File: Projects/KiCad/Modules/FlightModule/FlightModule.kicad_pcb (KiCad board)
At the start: 2 copper layers, 110 x 95 mm, 72 parts, among them J1 Conn_01x08, J2 Conn_01x02_Pin, J3 Conn_01x02_Pin, J4 Conn_01x02_Pin, J5 Conn_01x02_Pin, J6 Conn_01x02_Pin, Q1 Q_NPN_BEC, Q2 Q_NPN_BEC, SW1 SW_DIP_x02, U1 MCP2562-E-P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

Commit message: ブザーの回路を修正
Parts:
- moved BZ1 7.60 mm to (186.0, 85.7), turned to -90 degrees
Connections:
- BZ1 pad 2: GND -> Net-(BZ1-+)
- Q2 pad 3: +5V -> Net-(BZ1-+)
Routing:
- net +5V: track 110.7 -> 97.3 mm
- net Net-(BZ1-+): track 0.00 -> 9.17 mm

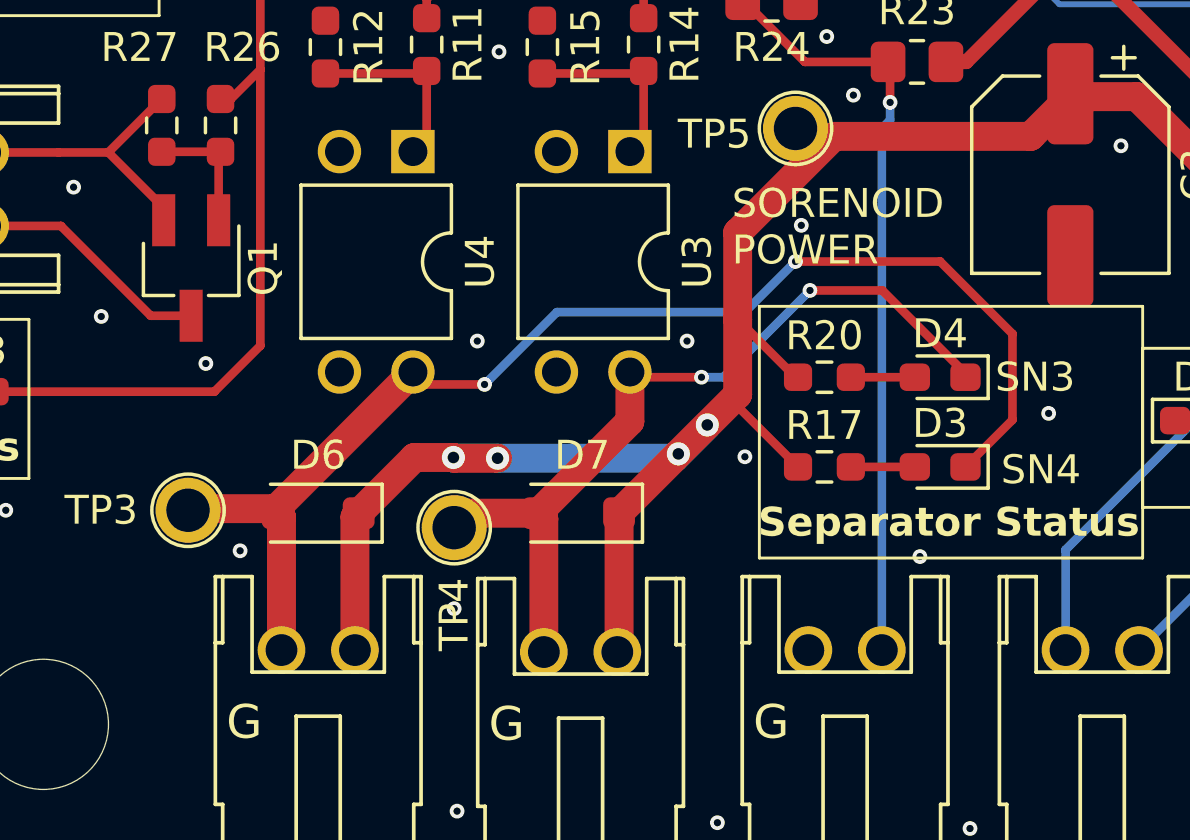
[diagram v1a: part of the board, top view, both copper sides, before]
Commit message: 電磁弁制御のフォトカプラの位置を修正
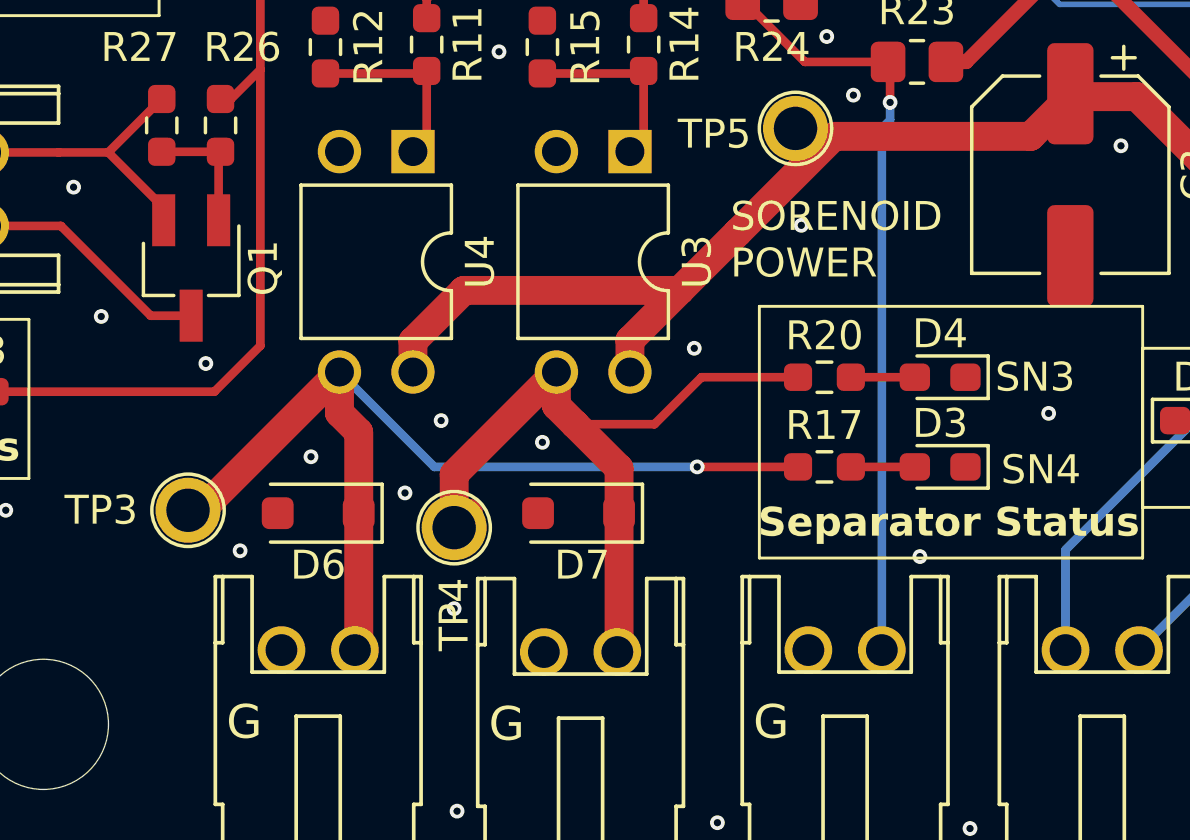
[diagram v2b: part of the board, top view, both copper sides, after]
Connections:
- D3 pad 1: Net-(D3-K) -> GND
- D4 pad 1: Net-(D4-K) -> GND
- D6 pad 1: SOLENOID_POWER -> Net-(D6-K)
- D6 pad 2: Net-(D3-K) -> GND
- D7 pad 1: SOLENOID_POWER -> Net-(D7-K)
- D7 pad 2: Net-(D4-K) -> GND
- J4 pad 1: Net-(D4-K) -> GND
- J4 pad 2: SOLENOID_POWER -> Net-(D7-K)
- J5 pad 1: Net-(D3-K) -> GND
- J5 pad 2: SOLENOID_POWER -> Net-(D6-K)
- R17 pad 1: SOLENOID_POWER -> Net-(D6-K)
- R20 pad 1: SOLENOID_POWER -> Net-(D7-K)
- TP3 pad 1: Net-(D3-K) -> Net-(D6-K)
- TP4 pad 1: Net-(D4-K) -> Net-(D7-K)
- U3 pad 3: GND -> Net-(D7-K)
- U3 pad 4: Net-(D4-K) -> SOLENOID_POWER
- U4 pad 3: GND -> Net-(D6-K)
- U4 pad 4: Net-(D3-K) -> SOLENOID_POWER
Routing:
- net Net-(D3-K): track 43.4 -> 0.00 mm, vias 2 -> 0
- net Net-(D6-K): track 0.00 -> 34.4 mm, vias 0 -> 1
- net Net-(D4-K): track 28.0 -> 0.00 mm, vias 2 -> 0
- net Net-(D7-K): track 0.00 -> 26.5 mm
- net SOLENOID_POWER: track 160.1 -> 135.9 mm, vias 4 -> 0
- net GND: vias 183 -> 185

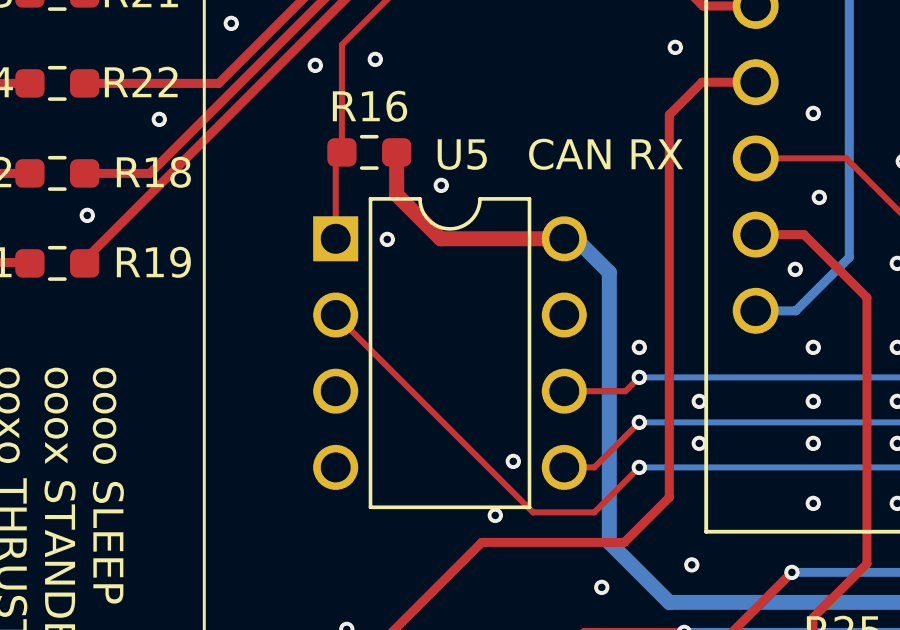
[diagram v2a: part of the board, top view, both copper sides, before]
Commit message: FRAMのWPとHOLDをHIGHに固定
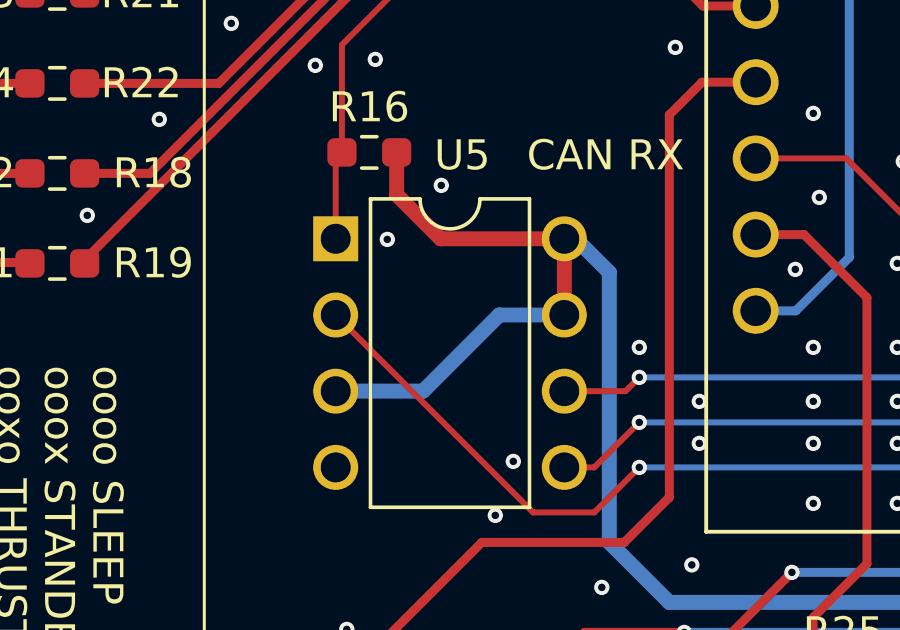
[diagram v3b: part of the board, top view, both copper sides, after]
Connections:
- U5 pad 3: GND -> +3.3V
- U5 pad 7: GND -> +3.3V
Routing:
- net +3.3V: track 86.9 -> 98.1 mm

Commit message: ガーバーを再生成
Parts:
- C1, C2, C4: value 0.1μF -> 0.1uF
- C3: value 47μF -> 47uF
- D1, D2: value ORANGE -> BLUE
- R1: value 120R1/4W -> 120R
- R10, R17, R20: value 2kΩ -> 2kR
- R11, R12, R14, R15: value 120Ω -> 120R
- R13, R18, R19, R21, R22: value 300Ω -> 300R
- R16, R26, R27, R30, R31: value 4.7kΩ -> 4.7kR
- R2, R7: value 820Ω -> 820R
- R23, R24: value 10kΩ -> 10kR
- R25: value 1kΩ -> 1kR
- R3: value 4.3kΩ -> 4.3kR
- R4: value 5.6kΩ -> 5.6kR
- R5, R6: value 100Ω -> 100R
- R8: value 750Ω -> 750R
- R9: value 3kΩ -> 3kR
- U3, U4: value TLP222A -> TLP241B
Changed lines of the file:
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@@
         (effects (font (size 1 1) (thickness 0.15)))
     )
-    (fp_text value "4.7kΩ" (at 0 1.43 90) (layer "F.Fab")
+    (fp_text value "4.7kR" (at 0 1.43 90) (layer "F.Fab")
         (effects (font (size 1 1) (thickness 0.15)))
     )
@@
         (effects (font (size 1 1) (thickness 0.153)))
     )
-    (fp_text value "4.3kΩ" (at 0 1.43) (layer "F.Fab")
+    (fp_text value "4.3kR" (at 0 1.43) (layer "F.Fab")
         (effects (font (size 1 1) (thickness 0.15)))
     )
@@
         (effects (font (size 1 1) (thickness 0.153)))
     )
-    (fp_text value "2kΩ" (at 0.0875 -1.5) (layer "F.Fab")
+    (fp_text value "2kR" (at 0.0875 -1.5) (layer "F.Fab")
         (effects (font (size 1 1) (thickness 0.15)))
     )
@@
         (effects (font (size 1 1) (thickness 0.153)))
     )
-    (fp_text value "120Ω" (at 0 1.43 90) (layer "F.Fab")
+    (fp_text value "120R" (at 0 1.43 90) (layer "F.Fab")
         (effects (font (size 1 1) (thickness 0.15)))
     )
@@
         (effects (font (size 1 1) (thickness 0.153)))
     )
-    (fp_text value "TLP222A" (at 3.81 4.87 90) (layer "F.Fab")
+    (fp_text value "TLP241B" (at 3.81 4.87 90) (layer "F.Fab")
         (effects (font (size 1 1) (thickness 0.15)))
     )
@@
         (effects (font (size 1 1) (thickness 0.153)))
     )
-    (fp_text value "750Ω" (at 0 1.43) (layer "F.Fab")
+    (fp_text value "750R" (at 0 1.43) (layer "F.Fab")
         (effects (font (size 1 1) (thickness 0.15)))
     )
@@
         (effects (font (size 1 1) (thickness 0.153)))
     )
-    (fp_text value "2kΩ" (at 0 1.43) (layer "F.Fab")
+    (fp_text value "2kR" (at 0 1.43) (layer "F.Fab")
         (effects (font (size 1 1) (thickness 0.15)))
     )
@@
         (effects (font (size 1 1) (thickness 0.153)))
     )
-    (fp_text value "TLP222A" (at 3.81 4.87 90) (layer "F.Fab")
+    (fp_text value "TLP241B" (at 3.81 4.87 90) (layer "F.Fab")
         (effects (font (size 1 1) (thickness 0.15)))
     )
@@
         (effects (font (size 1 1) (thickness 0.15)))
     )
-    (fp_text value "0.1μF" (at 0 1.43 90) (layer "F.Fab")
+    (fp_text value "0.1uF" (at 0 1.43 90) (layer "F.Fab")
         (effects (font (size 1 1) (thickness 0.15)))
     )
@@
         (effects (font (size 1 1) (thickness 0.153)))
     )
-    (fp_text value "300Ω" (at 0 1.43 180) (layer "F.Fab")
+    (fp_text value "300R" (at 0 1.43 180) (layer "F.Fab")
         (effects (font (size 1 1) (thickness 0.15)))
     )
@@
         (effects (font (size 1 1) (thickness 0.153)))
     )
-    (fp_text value "300Ω" (at 0 1.43 180) (layer "F.Fab")
+    (fp_text value "300R" (at 0 1.43 180) (layer "F.Fab")
         (effects (font (size 1 1) (thickness 0.15)))
     )
@@
         (effects (font (size 1 1) (thickness 0.153)))
     )
-    (fp_text value "300Ω" (at 0 1.43 180) (layer "F.Fab")
+    (fp_text value "300R" (at 0 1.43 180) (layer "F.Fab")
         (effects (font (size 1 1) (thickness 0.15)))
     )
@@
         (effects (font (size 1 1) (thickness 0.153)))
     )
-    (fp_text value "4.7kΩ" (at 0 1.43 180) (layer "F.Fab")
+    (fp_text value "4.7kR" (at 0 1.43 180) (layer "F.Fab")
         (effects (font (size 1 1) (thickness 0.15)))
     )
@@
         (effects (font (size 1 1) (thickness 0.153)))
     )
-    (fp_text value "1kΩ" (at 0 1.43) (layer "F.Fab")
+    (fp_text value "1kR" (at 0 1.43) (layer "F.Fab")
         (effects (font (size 1 1) (thickness 0.15)))
     )
@@
         (effects (font (size 1 1) (thickness 0.153)))
     )
-    (fp_text value "300Ω" (at -0.1 -1.5) (layer "F.Fab")
+    (fp_text value "300R" (at -0.1 -1.5) (layer "F.Fab")
         (effects (font (size 1 1) (thickness 0.15)))
     )
@@
         (effects (font (size 1 1) (thickness 0.153)))
     )
-    (fp_text value "ORANGE" (at 0 1.43) (layer "F.Fab")
+    (fp_text value "BLUE" (at 0 1.43) (layer "F.Fab")
         (effects (font (size 1 1) (thickness 0.15)))
     )
@@
         (effects (font (size 1 1) (thickness 0.15)))
     )
-    (fp_text value "0.1μF" (at 0 1.43 90) (layer "F.Fab")
+    (fp_text value "0.1uF" (at 0 1.43 90) (layer "F.Fab")
         (effects (font (size 1 1) (thickness 0.15)))
     )
@@
         (effects (font (size 1 1) (thickness 0.15)))
     )
-    (fp_text value "100Ω" (at 0 1.65) (layer "F.Fab")
+    (fp_text value "100R" (at 0 1.65) (layer "F.Fab")
         (effects (font (size 1 1) (thickness 0.15)))
     )
@@
         (effects (font (size 1 1) (thickness 0.153)))
     )
-    (fp_text value "ORANGE" (at 0 1.43) (layer "F.Fab")
+    (fp_text value "BLUE" (at 0 1.43) (layer "F.Fab")
         (effects (font (size 1 1) (thickness 0.15)))
     )
@@
         (effects (font (size 1 1) (thickness 0.153)))
     )
-    (fp_text value "120R1/4W" (at 0 1.43 90) (layer "F.Fab")
+    (fp_text value "120R" (at 0 1.43 90) (layer "F.Fab")
         (effects (font (size 1 1) (thickness 0.15)))
     )
@@
         (effects (font (size 1 1) (thickness 0.15)))
     )
-    (fp_text value "100Ω" (at 0 1.65) (layer "F.Fab")
+    (fp_text value "100R" (at 0 1.65) (layer "F.Fab")
         (effects (font (size 1 1) (thickness 0.15)))
     )
@@
         (effects (font (size 1 1) (thickness 0.15)))
     )
-    (fp_text value "0.1μF" (at 0 1.43) (layer "F.Fab")
+    (fp_text value "0.1uF" (at 0 1.43) (layer "F.Fab")
         (effects (font (size 1 1) (thickness 0.15)))
     )
@@
         (effects (font (size 1 1) (thickness 0.153)))
     )
-    (fp_text value "300Ω" (at 0 1.43 180) (layer "F.Fab")
+    (fp_text value "300R" (at 0 1.43 180) (layer "F.Fab")
         (effects (font (size 1 1) (thickness 0.15)))
     )
@@
         (effects (font (size 1 1) (thickness 0.153)))
     )
-    (fp_text value "2kΩ" (at 0 1.43) (layer "F.Fab")
+    (fp_text value "2kR" (at 0 1.43) (layer "F.Fab")
         (effects (font (size 1 1) (thickness 0.15)))
     )
@@
         (effects (font (size 1 1) (thickness 0.153)))
     )
-    (fp_text value "3kΩ" (at 0 1.43) (layer "F.Fab")
+    (fp_text value "3kR" (at 0 1.43) (layer "F.Fab")
         (effects (font (size 1 1) (thickness 0.15)))
     )
@@
         (effects (font (size 1 1) (thickness 0.153)))
     )
-    (fp_text value "5.6kΩ" (at 0 1.43) (layer "F.Fab")
+    (fp_text value "5.6kR" (at 0 1.43) (layer "F.Fab")
         (effects (font (size 1 1) (thickness 0.15)))
     )
@@
         (effects (font (size 1 1) (thickness 0.15)))
     )
-    (fp_text value "4.7kΩ" (at 0 1.43) (layer "F.Fab")
+    (fp_text value "4.7kR" (at 0 1.43) (layer "F.Fab")
         (effects (font (size 1 1) (thickness 0.15)))
     )
@@
         (effects (font (size 1 1) (thickness 0.153)))
     )
-    (fp_text value "120Ω" (at 0 1.43 90) (layer "F.Fab")
+    (fp_text value "120R" (at 0 1.43 90) (layer "F.Fab")
         (effects (font (size 1 1) (thickness 0.15)))
     )
@@
         (effects (font (size 1 1) (thickness 0.153)))
     )
-    (fp_text value "120Ω" (at 0 1.43 90) (layer "F.Fab")
+    (fp_text value "120R" (at 0 1.43 90) (layer "F.Fab")
         (effects (font (size 1 1) (thickness 0.15)))
     )
@@
         (effects (font (size 1 1) (thickness 0.15)))
     )
-    (fp_text value "10kΩ" (at 0 1.65 180) (layer "F.Fab")
+    (fp_text value "10kR" (at 0 1.65 180) (layer "F.Fab")
         (effects (font (size 1 1) (thickness 0.15)))
     )
@@
         (effects (font (size 1 1) (thickness 0.15)))
     )
-    (fp_text value "4.7kΩ" (at 0 1.43 90) (layer "F.Fab")
+    (fp_text value "4.7kR" (at 0 1.43 90) (layer "F.Fab")
         (effects (font (size 1 1) (thickness 0.15)))
     )
@@
         (effects (font (size 1 1) (thickness 0.153)))
     )
-    (fp_text value "820Ω" (at 0 1.43) (layer "F.Fab")
+    (fp_text value "820R" (at 0 1.43) (layer "F.Fab")
         (effects (font (size 1 1) (thickness 0.15)))
     )
@@
         (effects (font (size 1 1) (thickness 0.15)))
     )
-    (fp_text value "4.7kΩ" (at 0 1.43) (layer "F.Fab")
+    (fp_text value "4.7kR" (at 0 1.43) (layer "F.Fab")
         (effects (font (size 1 1) (thickness 0.15)))
     )
@@
         (effects (font (size 1 1) (thickness 0.153)))
     )
-    (fp_text value "820Ω" (at 0 1.43) (layer "F.Fab")
+    (fp_text value "820R" (at 0 1.43) (layer "F.Fab")
         (effects (font (size 1 1) (thickness 0.15)))
     )
@@
         (effects (font (size 1 1) (thickness 0.15)))
     )
-    (fp_text value "10kΩ" (at 0 1.65 180) (layer "F.Fab")
+    (fp_text value "10kR" (at 0 1.65 180) (layer "F.Fab")
         (effects (font (size 1 1) (thickness 0.15)))
     )
@@
         (effects (font (size 1 1) (thickness 0.153)))
     )
-    (fp_text value "120Ω" (at 0 1.43 90) (layer "F.Fab")
+    (fp_text value "120R" (at 0 1.43 90) (layer "F.Fab")
         (effects (font (size 1 1) (thickness 0.15)))
     )
@@
         (effects (font (size 1 1) (thickness 0.15)))
     )
-    (fp_text value "47μF" (at 0 4.35 -90) (layer "F.Fab")
+    (fp_text value "47uF" (at 0 4.35 -90) (layer "F.Fab")
         (effects (font (size 1 1) (thickness 0.15)))
     )

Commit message: QRと署名を更新
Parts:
- moved G*** 1.12 mm to (148.5, 60.0)
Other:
- board text added: "Flight Module Build 2"
- board text removed: "Flight Module Build 1"

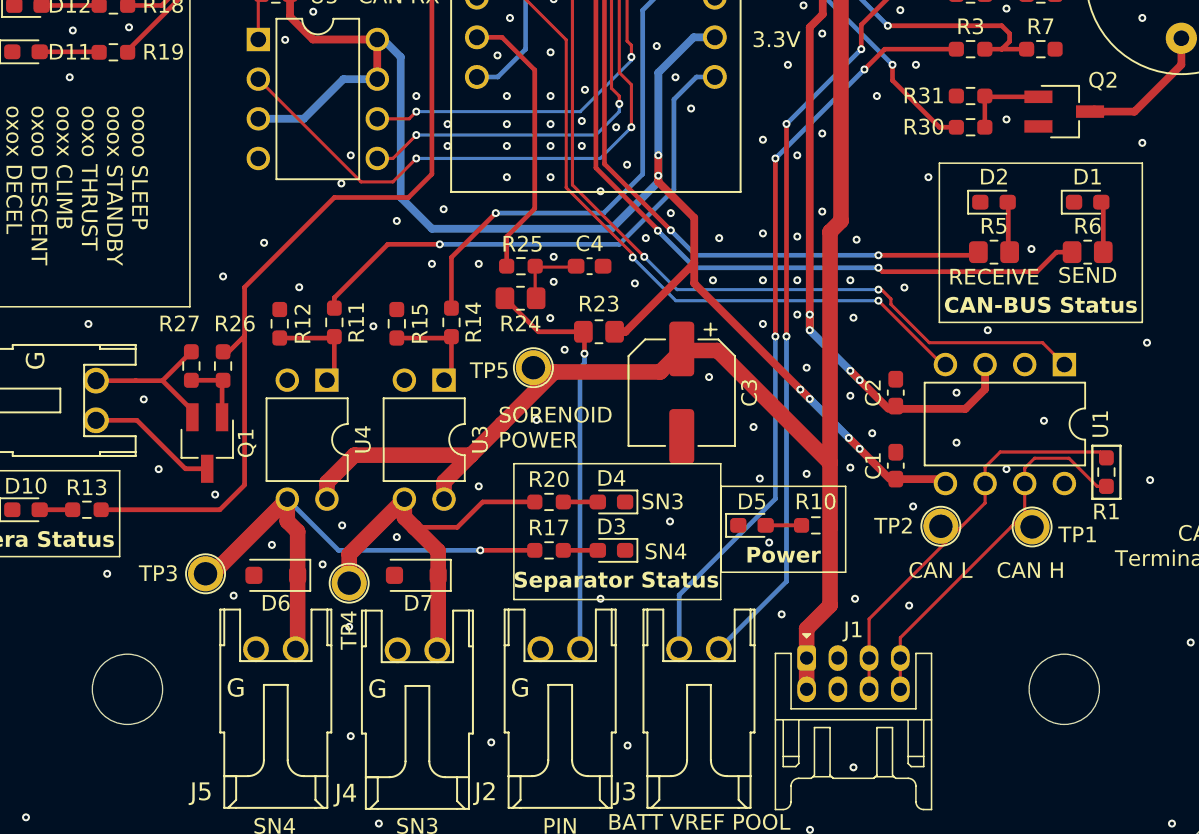
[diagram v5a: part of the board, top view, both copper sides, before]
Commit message: 分離制御回路を修正
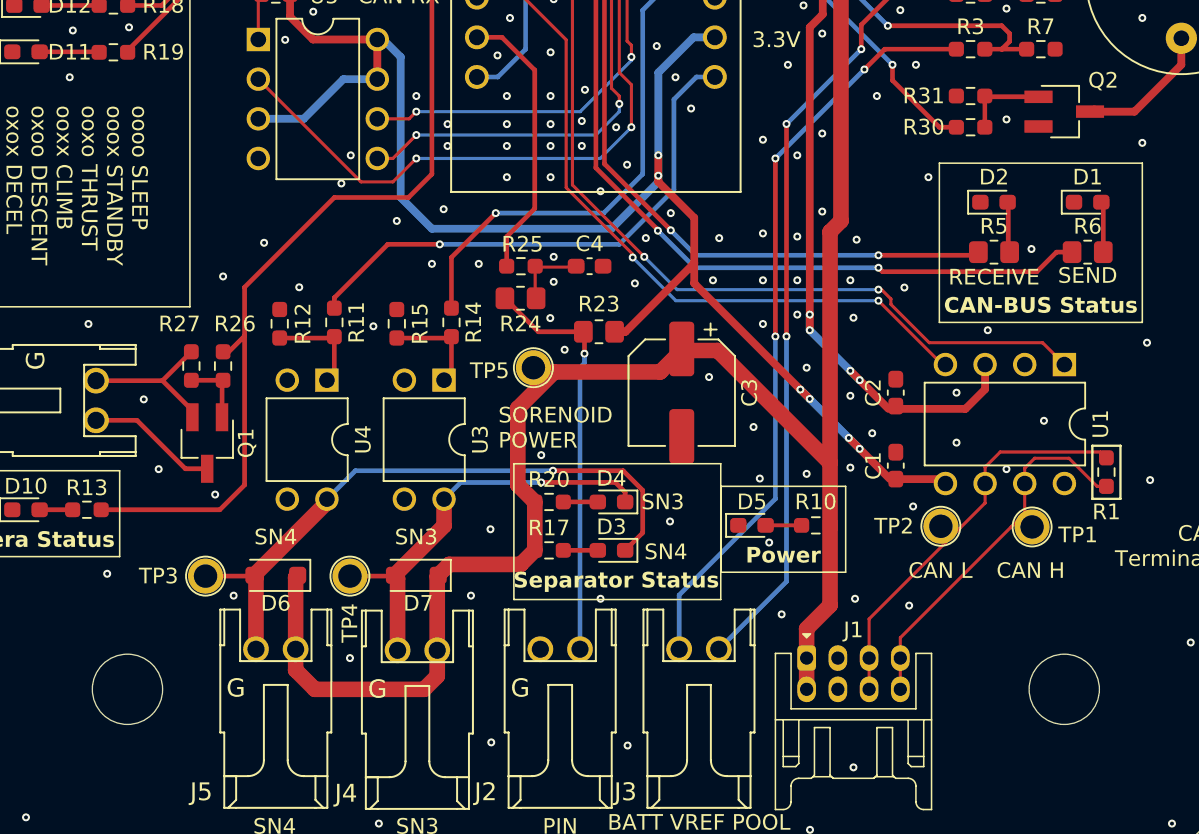
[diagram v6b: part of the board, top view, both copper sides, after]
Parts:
- moved TP4 0.45 mm to (132.8, 127.8)
- moved TP3 0.15 mm to (123.5, 127.8)
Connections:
- D3 pad 1: GND -> Net-(D3-K)
- D4 pad 1: GND -> Net-(D4-K)
- D6 pad 1: Net-(D6-K) -> SOLENOID_POWER
- D6 pad 2: GND -> Net-(D3-K)
- D7 pad 1: Net-(D7-K) -> SOLENOID_POWER
- D7 pad 2: GND -> Net-(D4-K)
- J4 pad 1: GND -> Net-(D4-K)
- J4 pad 2: Net-(D7-K) -> SOLENOID_POWER
- J5 pad 1: GND -> Net-(D3-K)
- J5 pad 2: Net-(D6-K) -> SOLENOID_POWER
- R17 pad 1: Net-(D6-K) -> SOLENOID_POWER
- R20 pad 1: Net-(D7-K) -> SOLENOID_POWER
- TP3 pad 1: Net-(D6-K) -> Net-(D3-K)
- TP4 pad 1: Net-(D7-K) -> Net-(D4-K)
- U3 pad 3: Net-(D7-K) -> GND
- U3 pad 4: SOLENOID_POWER -> Net-(D4-K)
- U4 pad 3: Net-(D6-K) -> GND
- U4 pad 4: SOLENOID_POWER -> Net-(D3-K)
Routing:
- net Net-(D3-K): track 0.00 -> 40.9 mm, vias 0 -> 1
- net Net-(D6-K): track 34.4 -> 0.00 mm, vias 1 -> 0
- net Net-(D4-K): track 0.00 -> 26.8 mm, vias 0 -> 1
- net Net-(D7-K): track 26.5 -> 0.00 mm
- net SOLENOID_POWER: track 135.9 -> 155.4 mm
- net GND: vias 185 -> 181
